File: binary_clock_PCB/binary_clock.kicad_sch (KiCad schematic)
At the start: 71 parts, among them J1 USB4105-GF-A, J2 uFL, J3 Conn_01x08_Socket, J4 JST-SM04B-SRSS, J5 JST-SM04B-SRSS, J6 JST-SM04B-SRSS, SW1 PTS636 SK25F, SW2 PTS636 SK25F, U1 ESP32-S3-WROOM-2-N32R8V, U2 AP2112K-3.3, U3 AP2112K-3.3, U4 MAX-M10S, U5 DS3231M, U6 VEML7700-TT, U7 SN74LVC1T45GW, U8 VEML7700-TT

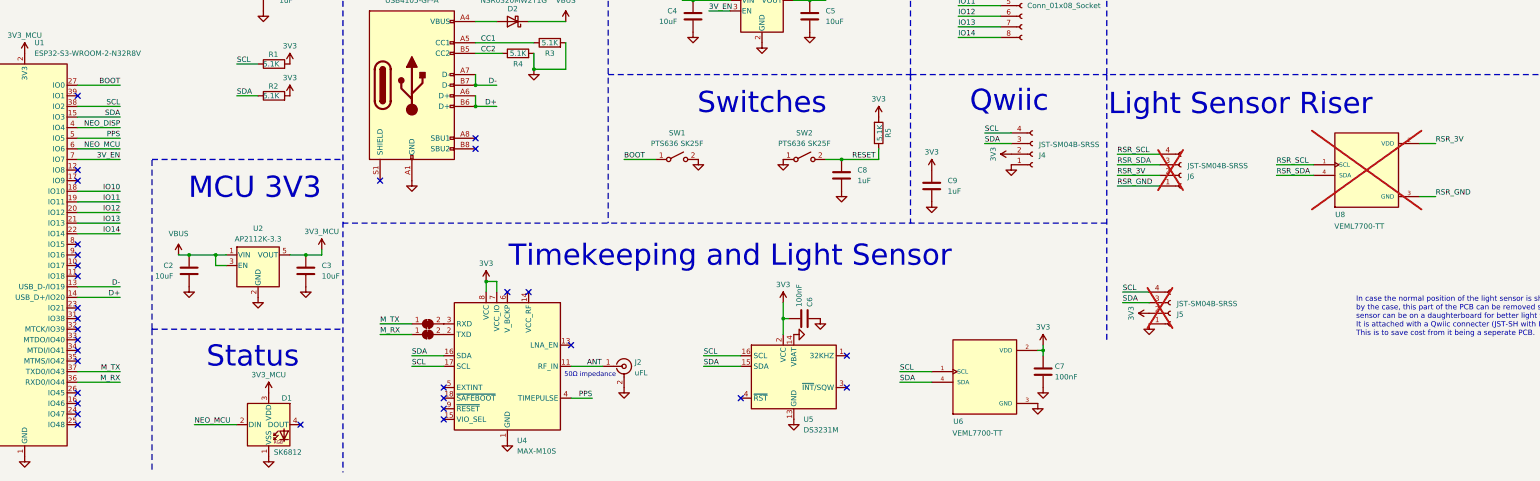
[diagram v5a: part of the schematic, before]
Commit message: Add final footprint positions
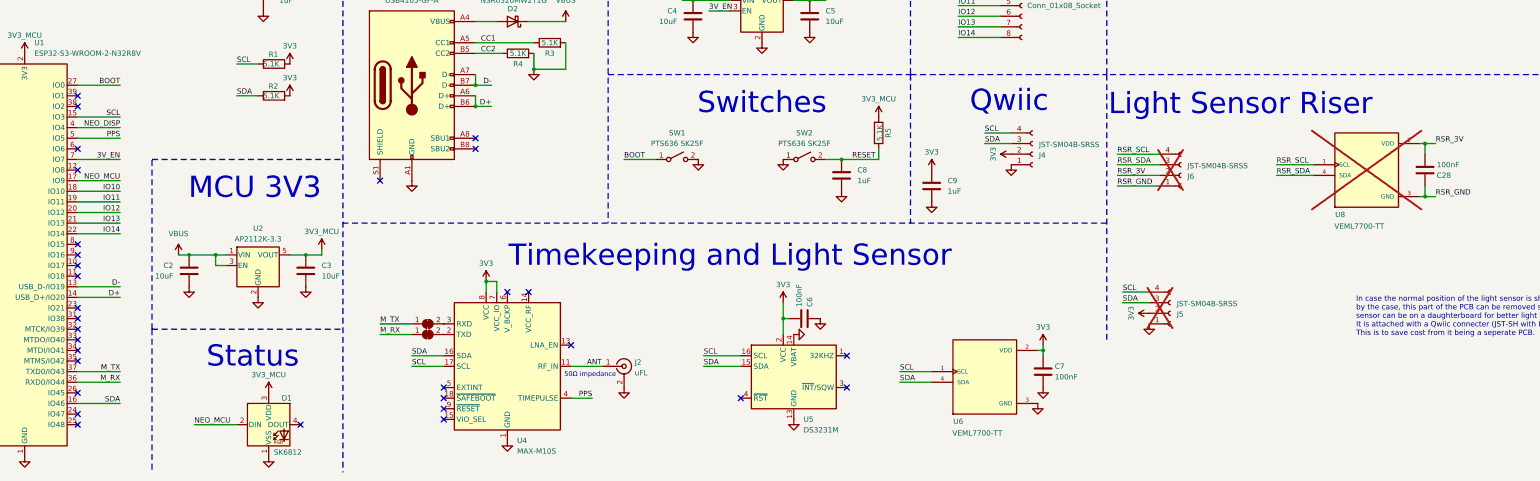
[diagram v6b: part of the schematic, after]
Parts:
- added C28: 100nF, Capacitor_SMD:C_0603_1608Metric, symbol Device:C
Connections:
- net 3V3: no longer R5.2
- net 3V3_MCU: now also R5.2
- net NEO_MCU: now also U1.17 (IO9); no longer U1.6 (IO6)
- net RSR_3V: now also C28.1
- net RSR_GND: now also C28.2
- net SCL: now also U1.15 (IO3); no longer U1.38 (IO2)
- net SDA: now also U1.16 (IO46); no longer U1.15 (IO3)
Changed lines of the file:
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@@
 	)
 	(junction
+		(at 375.92 205.74)
+		(diameter 0)
+		(color 0 0 0 0)
+	)
+	(junction
 		(at 185.42 27.94)
 		(diameter 0)
@@
 		(color 0 0 0 0)
 	)
-	(no_connect
-		(at 53.34 212.09)
+	(junction
+		(at 375.92 218.44)
+		(diameter 0)
+		(color 0 0 0 0)
 	)
 	(no_connect
@@
 	)
 	(no_connect
-		(at 53.34 214.63)
+		(at 53.34 232.41)
+	)
+	(no_connect
+		(at 53.34 273.05)
 	)
 	(no_connect
@@
 	)
 	(no_connect
-		(at 53.34 232.41)
-	)
-	(no_connect
 		(at 237.49 256.54)
 	)
@@
 	)
 	(no_connect
-		(at 53.34 265.43)
+		(at 383.54 35.56)
 	)
 	(no_connect
-		(at 383.54 35.56)
+		(at 53.34 207.01)
 	)
 	(no_connect
@@
 	)
 	(no_connect
-		(at 53.34 273.05)
-	)
-	(no_connect
 		(at 212.09 266.7)
 	)
@@
 	)
 	(no_connect
+		(at 53.34 212.09)
+	)
+	(no_connect
 		(at 156.21 241.3)
 	)
@@
 	)
 	(no_connect
-		(at 53.34 267.97)
+		(at 53.34 265.43)
 	)
 	(no_connect
@@
 	)
 	(no_connect
+		(at 53.34 196.85)
+	)
+	(no_connect
 		(at 53.34 255.27)
 	)
@@
 	(wire
 		(pts
-			(xy 148.59 191.77) (xy 153.67 191.77)
+			(xy 148.59 191.77) (xy 152.4 191.77)
 		)
 		(stroke
@@
 	(wire
 		(pts
+			(xy 375.92 205.74) (xy 375.92 208.28)
+		)
+		(stroke
+			(width 0)
+			(type default)
+		)
+	)
+	(wire
+		(pts
 			(xy 53.34 209.55) (xy 63.5 209.55)
 		)
@@
 	(wire
 		(pts
-			(xy 374.65 205.74) (xy 378.46 205.74)
+			(xy 374.65 205.74) (xy 375.92 205.74)
 		)
 		(stroke
@@
 	(wire
 		(pts
+			(xy 53.34 267.97) (xy 63.5 267.97)
+		)
+		(stroke
+			(width 0)
+			(type default)
+		)
+	)
+	(wire
+		(pts
 			(xy 125.73 248.92) (xy 133.35 248.92)
 		)
@@
 	(wire
 		(pts
-			(xy 86.36 234.95) (xy 86.36 232.41)
+			(xy 375.92 215.9) (xy 375.92 218.44)
 		)
 		(stroke
@@
 		)
 	)
-	(polyline
+	(wire
 		(pts
-			(xy 407.67 189.23) (xy 299.72 189.23)
+			(xy 86.36 234.95) (xy 86.36 232.41)
 		)
 		(stroke
 			(width 0)
-			(type dash)
+			(type default)
 		)
 	)
-	(wire
+	(polyline
 		(pts
-			(xy 242.57 43.18) (xy 261.62 43.18)
+			(xy 407.67 189.23) (xy 299.72 189.23)
 		)
 		(stroke
 			(width 0)
-			(type default)
+			(type dash)
 		)
 	)
 	(wire
 		(pts
-			(xy 33.02 43.18) (xy 52.07 43.18)
+			(xy 242.57 43.18) (xy 261.62 43.18)
 		)
 		(stroke
@@
 	(wire
 		(pts
-			(xy 53.34 196.85) (xy 63.5 196.85)
+			(xy 33.02 43.18) (xy 52.07 43.18)
 		)
 		(stroke
@@
 	(wire
 		(pts
-			(xy 154.94 35.56) (xy 158.75 35.56)
+			(xy 53.34 214.63) (xy 63.5 214.63)
 		)
 		(stroke
@@
 	(wire
 		(pts
-			(xy 274.32 170.18) (xy 264.16 170.18)
+			(xy 154.94 35.56) (xy 158.75 35.56)
 		)
 		(stroke
@@
 	(wire
 		(pts
-			(xy 53.34 207.01) (xy 63.5 207.01)
+			(xy 274.32 170.18) (xy 264.16 170.18)
 		)
 		(stroke
@@
 	(wire
 		(pts
-			(xy 374.65 218.44) (xy 378.46 218.44)
+			(xy 53.34 217.17) (xy 63.5 217.17)
 		)
 		(stroke
@@
 	(wire
 		(pts
-			(xy 53.34 217.17) (xy 63.5 217.17)
+			(xy 299.72 43.18) (xy 318.77 43.18)
 		)
 		(stroke
@@
 	(wire
 		(pts
-			(xy 299.72 43.18) (xy 318.77 43.18)
+			(xy 375.92 218.44) (xy 378.46 218.44)
 		)
 		(stroke
@@
 	(wire
 		(pts
-			(xy 53.34 199.39) (xy 63.5 199.39)
-		)
-		(stroke
-			(width 0)
-			(type default)
-		)
-	)
-	(wire
-		(pts
 			(xy 53.34 227.33) (xy 63.5 227.33)
 		)
@@
 	(wire
 		(pts
-			(xy 148.59 196.85) (xy 153.67 196.85)
+			(xy 148.59 196.85) (xy 152.4 196.85)
 		)
 		(stroke
@@
 		)
 	)
+	(wire
+		(pts
+			(xy 53.34 199.39) (xy 63.5 199.39)
+		)
+		(stroke
+			(width 0)
+			(type default)
+		)
+	)
 	(polyline
 		(pts
@@
 	(wire
 		(pts
+			(xy 374.65 218.44) (xy 375.92 218.44)
+		)
+		(stroke
+			(width 0)
+			(type default)
+		)
+	)
+	(wire
+		(pts
 			(xy 231.14 35.56) (xy 234.95 35.56)
 		)
@@
 	(wire
 		(pts
+			(xy 375.92 205.74) (xy 378.46 205.74)
+		)
+		(stroke
+			(width 0)
+			(type default)
+		)
+	)
+	(wire
+		(pts
 			(xy 274.32 177.8) (xy 264.16 177.8)
 		)
@@
 	)
 	(label "D+"
-		(at 153.67 196.85 180)
+		(at 152.4 196.85 180)
 		(fields_autoplaced yes)
 		(effects
@@
 		)
 	)
+	(label "NEO_MCU"
+		(at 63.5 214.63 180)
+		(fields_autoplaced yes)
+		(effects
+			(font
+				(size 1.27 1.27)
+			)
+			(justify right bottom)
+		)
+	)
 	(label "VBUS"
 		(at 46.99 27.94 0)
@@
 	)
 	(label "SCL"
-		(at 63.5 196.85 180)
+		(at 63.5 199.39 180)
 		(fields_autoplaced yes)
 		(effects
@@
 	)
 	(label "SDA"
-		(at 63.5 199.39 180)
+		(at 63.5 267.97 180)
 		(fields_autoplaced yes)
 		(effects
@@
 	)
 	(label "D-"
-		(at 153.67 191.77 180)
+		(at 152.4 191.77 180)
 		(fields_autoplaced yes)
 		(effects
@@
 		)
 	)
-	(label "NEO_MCU"
-		(at 63.5 207.01 180)
-		(fields_autoplaced yes)
-		(effects
-			(font
-				(size 1.27 1.27)
-			)
-			(justify right bottom)
-		)
-	)
 	(label "RSR_GND"
 		(at 302.26 215.9 0)
@@
 			)
 		)
-		(property "Value" "3V3"
+		(property "Value" "3V3_MCU"
 			(at 245.11 195.072 0)
 			(effects
@@
 					(unit 1)
 				)
+			)
+		)
+	)
+	(symbol
+		(lib_id "Device:C")
+		(at 375.92 212.09 0)
+		(mirror y)
+		(unit 1)
+		(exclude_from_sim no)
+		(in_bom yes)
+		(on_board yes)
+		(dnp no)
+		(property "Reference" "C28"
+			(at 378.714 213.36 0)
+			(effects
+				(font
+					(size 1.27 1.27)
+				)
+				(justify right)
+			)
+		)
+		(property "Value" "100nF"
+			(at 378.714 210.82 0)
+			(effects
+				(font
+					(size 1.27 1.27)
+				)
+				(justify right)
+			)
+		)
+		(property "Footprint" "Capacitor_SMD:C_0603_1608Metric"
+			(at 374.9548 215.9 0)
+			(effects
+				(font
+					(size 1.27 1.27)
+				)
+				(hide yes)
+			)
+		)
+		(property "Datasheet" "~"
+			(at 375.92 212.09 0)
+			(effects
+				(font
+					(size 1.27 1.27)
+				)
+				(hide yes)
+			)
+		)
+		(property "Description" "Unpolarized capacitor"
+			(at 375.92 212.09 0)
+			(effects
+				(font
+					(size 1.27 1.27)
+				)
+				(hide yes)
+			)
+		)
+		(pin "2"
+		)
+		(pin "1"
+		)
+		(instances
+			(project "binary_clock"
+				(path "/6e85e51c-9ae3-4e5c-b193-13cd65a7b908"
+					(reference "C28")
+					(unit 1)
+				)

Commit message: Change schematic, start routing
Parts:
- removed JP1, JP2: SolderJumper_2_Bridged, besser_footprints:solder_jumper_bridged, symbol Jumper:SolderJumper_2_Bridged
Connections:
- net 3V3: no longer C1.1
- net 3V3_MCU: now also C1.1
- net NEO_DISP: now also U1.31 (IO38); no longer U1.4 (IO4)
- net PPS: now also U1.15 (IO3); no longer U1.5 (IO5)
- net SCL: now also U1.33 (MTDO/IO40); no longer U1.15 (IO3)
- net SDA: now also U1.32 (MTCK/IO39); no longer U1.16 (IO46)
- net VBUS: now also U3.3 (EN)
- net 3V_EN: no longer names the net of U1.7 (IO7)
- net 3V_EN: no longer U3.3 (EN)
- net M_RX: no longer names the net of U1.36 (RXD0/IO44)
- net M_TX: no longer names the net of U1.37 (TXD0/IO43)
- no-connect marks 32 -> 37
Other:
- note removed: "Try to compile custom CircuitPython build so that things like blinking red neopixel on error works, and being able to toggle I2C LDO (on by default, but can be turned off in code). https://learn.adafruit.com/how-to-add-a-new-board-to-circuitpython/customizing-the-board-files"

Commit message: Almost finish placements
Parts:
- C2, C3, C4, C5: value 10uF -> 1uF
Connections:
- net 3V3: now also J3.2 (Pin_2); no longer J3.3 (Pin_3)
- net PPS: now also U1.34 (MTDI/IO41); no longer U1.15 (IO3)
- net VBUS: now also J3.3 (Pin_3); no longer J3.2 (Pin_2)
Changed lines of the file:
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@@
 	)
 	(no_connect
-		(at 53.34 255.27)
+		(at 53.34 207.01)
 	)
 	(no_connect
-		(at 53.34 207.01)
+		(at 53.34 199.39)
 	)
 	(no_connect
@@
 	(wire
 		(pts
+			(xy 63.5 255.27) (xy 53.34 255.27)
+		)
+		(stroke
+			(width 0)
+			(type default)
+		)
+	)
+	(wire
+		(pts
 			(xy 284.48 256.54) (xy 284.48 255.27)
 		)
@@
 	(wire
 		(pts
-			(xy 53.34 199.39) (xy 63.5 199.39)
-		)
-		(stroke
-			(width 0)
-			(type default)
-		)
-	)
-	(wire
-		(pts
 			(xy 269.24 35.56) (xy 273.05 35.56)
 		)
@@
 	)
 	(label "PPS"
-		(at 63.5 199.39 180)
+		(at 63.5 255.27 180)
 		(fields_autoplaced yes)
 		(effects
@@
 		)
 	)
-	(label "VBUS"
+	(label "3V3"
 		(at 264.16 165.1 0)
 		(fields_autoplaced yes)
@@
 		)
 	)
-	(label "3V3"
+	(label "VBUS"
 		(at 264.16 167.64 0)
 		(fields_autoplaced yes)
@@
 			)
 		)
-		(property "Value" "10uF"
+		(property "Value" "1uF"
 			(at 76.2 237.4899 0)
 			(effects
@@
 			)
 		)
-		(property "Value" "10uF"
+		(property "Value" "1uF"
 			(at 232.41 176.53 0)
 			(effects
@@
 			)
 		)
-		(property "Value" "10uF"
+		(property "Value" "1uF"
 			(at 111.76 237.49 0)
 			(effects
@@
 			)
 		)
-		(property "Value" "10uF"
+		(property "Value" "1uF"
 			(at 196.85 176.5299 0)
 			(effects
